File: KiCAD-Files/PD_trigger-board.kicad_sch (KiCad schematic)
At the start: 25 parts, among them J1 USB_C_Receptacle_USB2.0_14P, J10 15V, J11 18V, J2 Conn_01x03, J3 Conn_01x03, J4 VOUT, J5 5V, J6 5V, J7 5V, J8 9V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

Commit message: Routin fertig
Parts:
- removed Q1: AONR21307, Adafruit HUSB238 USB-C PD Breakout:POWERDI3333, symbol Adafruit HUSB238 USB-C PD Breakout-eagle-import:MOSFET-P-POWERDI3333
- added U2: SI4459ADY-T1-GE3, blinkyparts:SO_ADY-T1-GE3_VIS, symbol SI4459ADY:SI4459ADY-T1-GE3
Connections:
- net VBUS: now also U2.1 (S), U2.2 (S), U2.3 (S)
- net VOUT: now also U2.5 (D), U2.6 (D), U2.7 (D), U2.8 (D)
- net at R3.2, R4.1: now also U2.4 (G)
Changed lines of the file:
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@@
 	(paper "A4")
+	(junction
+		(at 236.22 105.41)
+		(diameter 0)
+		(color 0 0 0 0)
+	)
+	(junction
+		(at 236.22 35.56)
+		(diameter 0)
+		(color 0 0 0 0)
+	)
+	(junction
+		(at 274.32 87.63)
+		(diameter 0)
+		(color 0 0 0 0)
+	)
+	(junction
+		(at 254 35.56)
+		(diameter 0)
+		(color 0 0 0 0)
+	)
+	(junction
+		(at 274.32 96.52)
+		(diameter 0)
+		(color 0 0 0 0)
+	)
+	(junction
+		(at 236.22 87.63)
+		(diameter 0)
+		(color 0 0 0 0)
+	)
+	(junction
+		(at 175.26 138.43)
+		(diameter 0)
+		(color 0 0 0 0)
+	)
+	(junction
+		(at 274.32 105.41)
+		(diameter 0)
+		(color 0 0 0 0)
+	)
+	(junction
+		(at 55.88 88.9)
+		(diameter 0)
+		(color 0 0 0 0)
+	)
+	(junction
+		(at 148.59 127)
+		(diameter 0)
+		(color 0 0 0 0)
+	)
+	(junction
+		(at 226.06 45.72)
+		(diameter 0)
+		(color 0 0 0 0)
+	)
+	(junction
+		(at 243.84 35.56)
+		(diameter 0)
+		(color 0 0 0 0)
+	)
 	(junction
 		(at 214.63 35.56)
@@
 	)
 	(junction
-		(at 236.22 105.41)
-		(diameter 0)
-		(color 0 0 0 0)
-	)
-	(junction
-		(at 274.32 87.63)
-		(diameter 0)
-		(color 0 0 0 0)
-	)
-	(junction
-		(at 254 35.56)
-		(diameter 0)
-		(color 0 0 0 0)
-	)
-	(junction
-		(at 274.32 96.52)
-		(diameter 0)
-		(color 0 0 0 0)
-	)
-	(junction
-		(at 236.22 87.63)
-		(diameter 0)
-		(color 0 0 0 0)
-	)
-	(junction
-		(at 175.26 138.43)
-		(diameter 0)
-		(color 0 0 0 0)
-	)
-	(junction
-		(at 274.32 105.41)
-		(diameter 0)
-		(color 0 0 0 0)
-	)
-	(junction
-		(at 55.88 88.9)
-		(diameter 0)
-		(color 0 0 0 0)
-	)
-	(junction
-		(at 148.59 127)
+		(at 220.98 33.02)
 		(diameter 0)
 		(color 0 0 0 0)
@@
 	)
 	(junction
+		(at 236.22 30.48)
+		(diameter 0)
+		(color 0 0 0 0)
+	)
+	(junction
 		(at 264.16 35.56)
 		(diameter 0)
@@
 	)
 	(junction
-		(at 243.84 35.56)
+		(at 220.98 35.56)
 		(diameter 0)
 		(color 0 0 0 0)
@@
 	)
 	(junction
-		(at 226.06 45.72)
+		(at 236.22 33.02)
 		(diameter 0)
 		(color 0 0 0 0)
@@
 	(wire
 		(pts
+			(xy 220.98 33.02) (xy 220.98 35.56)
+		)
+		(stroke
+			(width 0)
+			(type default)
+		)
+	)
+	(wire
+		(pts
 			(xy 255.27 115.57) (xy 274.32 115.57)
 		)
@@
 	(wire
 		(pts
+			(xy 236.22 30.48) (xy 236.22 33.02)
+		)
+		(stroke
+			(width 0)
+			(type default)
+		)
+	)
+	(wire
+		(pts
 			(xy 148.59 120.65) (xy 148.59 127)
 		)
@@
 	(wire
 		(pts
+			(xy 236.22 33.02) (xy 236.22 35.56)
+		)
+		(stroke
+			(width 0)
+			(type default)
+		)
+	)
+	(wire
+		(pts
 			(xy 81.28 152.4) (xy 83.82 152.4)
 		)
@@
 	(wire
 		(pts
+			(xy 220.98 30.48) (xy 220.98 33.02)
+		)
+		(stroke
+			(width 0)
+			(type default)
+		)
+	)
+	(wire
+		(pts
 			(xy 236.22 87.63) (xy 236.22 96.52)
 		)
@@
 	(wire
 		(pts
+			(xy 236.22 27.94) (xy 236.22 30.48)
+		)
+		(stroke
+			(width 0)
+			(type default)
+		)
+	)
+	(wire
+		(pts
 			(xy 246.38 115.57) (xy 252.73 115.57)
 		)
@@
 	(wire
 		(pts
-			(xy 214.63 35.56) (xy 223.52 35.56)
+			(xy 226.06 40.64) (xy 226.06 45.72)
 		)
 		(stroke
@@
 	(wire
 		(pts
-			(xy 233.68 35.56) (xy 243.84 35.56)
-		)
-		(stroke
-			(width 0)
-			(type default)
-		)
-	)
-	(wire
-		(pts
 			(xy 236.22 105.41) (xy 236.22 115.57)
 		)
@@
 	(wire
 		(pts
+			(xy 236.22 35.56) (xy 243.84 35.56)
+		)
+		(stroke
+			(width 0)
+			(type default)
+		)
+	)
+	(wire
+		(pts
 			(xy 274.32 105.41) (xy 274.32 96.52)
 		)
@@
 	(wire
 		(pts
-			(xy 226.06 40.64) (xy 226.06 45.72)
-		)
-		(stroke
-			(width 0)
-			(type default)
-		)
-	)
-	(wire
-		(pts
 			(xy 264.16 35.56) (xy 273.05 35.56)
 		)
@@
 		(pts
 			(xy 130.81 80.01) (xy 130.81 82.55)
+		)
+		(stroke
+			(width 0)
+			(type default)
+		)
+	)
+	(wire
+		(pts
+			(xy 214.63 35.56) (xy 220.98 35.56)
 		)
 		(stroke
@@
 	)
 	(symbol
-		(lib_id "Adafruit HUSB238 USB-C PD Breakout-eagle-import:MOSFET-P-POWERDI3333")
-		(at 228.6 35.56 90)
-		(unit 1)
-		(exclude_from_sim no)
-		(in_bom yes)
-		(on_board yes)
-		(dnp no)
-		(property "Reference" "Q1"
-			(at 228.219 32.766 0)
-			(effects
-				(font
-					(size 1.27 1.0795)
-				)
-				(justify left bottom)
-			)
-		)
-		(property "Value" "AONR21307"
-			(at 230.505 32.766 0)
-			(effects
-				(font
-					(size 1.27 1.0795)
-				)
-				(justify left bottom)
-			)
-		)
-		(property "Footprint" "Adafruit HUSB238 USB-C PD Breakout:POWERDI3333"
-			(at 228.6 35.56 0)
-			(effects
-				(font
-					(size 1.27 1.27)
-				)
-				(hide yes)
-			)
-		)
-		(property "Datasheet" ""
-			(at 228.6 35.56 0)
-			(effects
-				(font
-					(size 1.27 1.27)
-				)
-				(hide yes)
-			)
-		)
-		(property "Description" ""
-			(at 228.6 35.56 0)
-			(effects
-				(font
-					(size 1.27 1.27)
-				)
-				(hide yes)
-			)
-		)
-		(pin "1"
-		)
-		(pin "2"
-		)
-		(pin "3"
-		)
-		(pin "4"
-		)
-		(pin "5678"
-		)
-		(instances
-			(project "PD_trigger-board"
-				(path "/e428d426-38f9-47e3-9715-a18ed772a1ec"
-					(reference "Q1")
-					(unit 1)
-				)
-			)
-		)
-	)
-	(symbol
 		(lib_id "power:GND")
 		(at 85.09 184.15 0)
@@
 					(unit 1)
 				)
+			)
+		)
+	)
+	(symbol
+		(lib_id "SI4459ADY:SI4459ADY-T1-GE3")
+		(at 226.06 40.64 90)
+		(unit 1)
+		(exclude_from_sim no)
+		(in_bom yes)
+		(on_board yes)
+		(dnp no)
+		(fields_autoplaced yes)
+		(property "Reference" "U2"
+			(at 228.6 22.86 90)
+			(effects
+				(font
+					(size 1.524 1.524)
+				)
+			)
+		)
+		(property "Value" "SI4459ADY-T1-GE3"
+			(at 228.6 25.4 90)
+			(effects
+				(font
+					(size 1.524 1.524)
+				)
+			)
+		)
+		(property "Footprint" "blinkyparts:SO_ADY-T1-GE3_VIS"
+			(at 226.06 40.64 0)
+			(effects
+				(font
+					(size 1.27 1.27)
+					(italic yes)
+				)
+				(hide yes)
+			)
+		)
+		(property "Datasheet" "SI4459ADY-T1-GE3"
+			(at 226.06 40.64 0)
+			(effects
+				(font
+					(size 1.27 1.27)
+					(italic yes)
+				)
+				(hide yes)
+			)
+		)
+		(property "Description" ""
+			(at 226.06 40.64 0)
+			(effects
+				(font
+					(size 1.27 1.27)
+				)
+				(hide yes)
+			)
+		)
+		(pin "2"
+		)
+		(pin "4"
+		)
+		(pin "1"
+		)
+		(pin "7"
+		)
+		(pin "6"
+		)
+		(pin "5"
+		)
+		(pin "3"
+		)
+		(pin "8"
+		)
+		(instances
+			(project ""
+				(path "/e428d426-38f9-47e3-9715-a18ed772a1ec"
+					(reference "U2")
+					(unit 1)
+				)

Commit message: Partlist fertig
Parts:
- C1: FCSC (none) -> C15849
- C2, C3, C4: value C -> 4.7uF 35V; FCSC (none) -> C307467
- J1: value USB_C_Receptacle_USB2.0_14P -> USB_C_Receptacle_USB3.0_12P
- R1: FCSC (none) -> C25139
- R2, R7: FCSC (none) -> C54831
- R3: FCSC (none) -> C100457
- R4: FCSC (none) -> C25941
- R5: value 6k -> 6.04k; FCSC (none) -> C25913
- R6: FCSC (none) -> C25531
- R8: FCSC (none) -> C25542
- U1: FCSC (none) -> C7471904
- U2: FCSC (none) -> C143743
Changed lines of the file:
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@@
+			)
+		)
+		(property "FCSC" "C25531"
+			(at 242.57 96.52 90)
+			(effects
+				(font
+					(size 1.27 1.27)
+				)
+				(hide yes)
 			)
 		)
@@
 			)
 		)
-		(property "Value" "C"
+		(property "Value" "4.7uF 35V"
 			(at 257.81 40.6399 0)
 			(effects
@@
 			)
 		)
+		(property "FCSC" "C307467"
+			(at 254 39.37 0)
+			(effects
+				(font
+					(size 1.27 1.27)
+				)
+				(hide yes)
+			)
+		)
 		(pin "1"
 		)
@@
 			)
 		)
+		(property "FCSC" "C25941"
+			(at 226.06 52.07 0)
+			(effects
+				(font
+					(size 1.27 1.27)
+				)
+				(hide yes)
+			)
+		)
 		(pin "2"
 		)
@@
 			)
 		)
+		(property "FCSC" "C100457"
+			(at 214.63 41.91 0)
+			(effects
+				(font
+					(size 1.27 1.27)
+				)
+				(hide yes)
+			)
+		)
 		(pin "2"
 		)
@@
 			)
 		)
-		(property "Value" "C"
+		(property "Value" "4.7uF 35V"
 			(at 247.65 40.6399 0)
 			(effects
@@
 			)
 		)
+		(property "FCSC" "C307467"
+			(at 243.84 39.37 0)
+			(effects
+				(font
+					(size 1.27 1.27)
+				)
+				(hide yes)
+			)
+		)
 		(pin "1"
 		)
@@
 			)
 		)
-		(property "Value" "USB_C_Receptacle_USB2.0_14P"
+		(property "Value" "USB_C_Receptacle_USB3.0_12P"
 			(at 40.64 64.77 0)
 			(effects
@@
 			)
 		)
-		(property "Description" "USB 2.0-only 14P Type-C Receptacle connector"
-			(at 40.64 85.09 0)
-			(effects
-				(font
-					(size 1.27 1.27)
-				)
-				(hide yes)
-			)
-		)
-		(property "LCSC" ""
+		(property "Description" "USB 3.0-only 12P Type-C Receptacle connector"
 			(at 40.64 85.09 0)
 			(effects
@@
 			)
 		)
-		(property "Description" ""
+		(property "Description" "P-Channel MOSFET"
 			(at 226.06 40.64 0)
+			(effects
+				(font
+					(size 1.27 1.27)
+				)
+				(hide yes)
+			)
+		)
+		(property "FCSC" "C143743"
+			(at 226.06 40.64 90)
 			(effects
 				(font
@@
 			)
 		)
+		(property "FCSC" "C7471904"
+			(at 170.18 88.9 0)
+			(effects
+				(font
+					(size 1.27 1.27)
+				)
+				(hide yes)
+			)
+		)
 		(pin "8"
 		)
@@
 			)
 		)
-		(property "Value" "C"
+		(property "Value" "4.7uF 35V"
 			(at 267.97 40.6399 0)
 			(effects
@@
 			)
 		)
+		(property "FCSC" "C307467"
+			(at 264.16 39.37 0)
+			(effects
+				(font
+					(size 1.27 1.27)
+				)
+				(hide yes)
+			)
+		)
 		(pin "1"
 		)
@@
 			)
 		)
+		(property "FCSC" "C25542"
+			(at 242.57 115.57 90)
+			(effects
+				(font
+					(size 1.27 1.27)
+				)
+				(hide yes)
+			)
+		)
 		(pin "2"
 		)
@@
 			)
 		)
+		(property "FCSC" "C15849"
+			(at 130.81 76.2 0)
+			(effects
+				(font
+					(size 1.27 1.27)
+				)
+				(hide yes)
+			)
+		)
 		(pin "1"
 		)
@@
 			)
 		)
+		(property "FCSC" "C54831"
+			(at 242.57 105.41 90)
+			(effects
+				(font
+					(size 1.27 1.27)
+				)
+				(hide yes)
+			)
+		)
 		(pin "2"
 		)
@@
 			)
 		)
+		(property "FCSC" "C25139"
+			(at 130.81 64.77 0)
+			(effects
+				(font
+					(size 1.27 1.27)
+				)
+				(hide yes)
+			)
+		)
 		(pin "2"
 		)
@@
 			)
 		)
-		(property "Value" "6k"
+		(property "Value" "6.04k"
 			(at 242.57 83.82 90)
 			(effects
@@
 			)
 		)
+		(property "FCSC" "C25913"
+			(at 242.57 87.63 90)
+			(effects
+				(font
+					(size 1.27 1.27)
+				)
+				(hide yes)
+			)
+		)
 		(pin "2"
 		)
@@
 			(effects
 				(font
+					(size 1.27 1.27)
+				)
+				(hide yes)
+			)
+		)
+		(property "FCSC" "C54831"
+			(at 156.21 138.43 90)
+			(effects
+				(font

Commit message: minor changes for v0.1
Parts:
- J1: FCSC (none) -> C136423
- J10, J11, J2, J3, J4, J5, J6, J7, J8, J9: now not fitted
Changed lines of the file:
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@@
 		(in_bom yes)
 		(on_board yes)
-		(dnp no)
+		(dnp yes)
 		(fields_autoplaced yes)
 		(property "Reference" "J7"
@@
 			)
 		)
+		(property "FCSC" "C136423"
+			(at 40.64 85.09 0)
+			(effects
+				(font
+					(size 1.27 1.27)
+				)
+				(hide yes)
+			)
+		)
 		(pin "A6"
 		)
@@
 		(in_bom yes)
 		(on_board yes)
-		(dnp no)
+		(dnp yes)
 		(fields_autoplaced yes)
 		(property "Reference" "J3"
@@
 		(in_bom yes)
 		(on_board yes)
-		(dnp no)
+		(dnp yes)
 		(fields_autoplaced yes)
 		(property "Reference" "J2"
@@
 		(in_bom yes)
 		(on_board yes)
-		(dnp no)
+		(dnp yes)
 		(fields_autoplaced yes)
 		(property "Reference" "J8"
@@
 		(in_bom yes)
 		(on_board yes)
-		(dnp no)
+		(dnp yes)
 		(fields_autoplaced yes)
 		(property "Reference" "J11"
@@
 		(in_bom yes)
 		(on_board yes)
-		(dnp no)
+		(dnp yes)
 		(fields_autoplaced yes)
 		(property "Reference" "J5"
@@
 		(in_bom yes)
 		(on_board yes)
-		(dnp no)
+		(dnp yes)
 		(fields_autoplaced yes)
 		(property "Reference" "J9"
@@
 		(in_bom yes)
 		(on_board yes)
-		(dnp no)
+		(dnp yes)
 		(fields_autoplaced yes)
 		(property "Reference" "J6"
@@
 		(in_bom yes)
 		(on_board yes)
-		(dnp no)
+		(dnp yes)
 		(fields_autoplaced yes)
 		(property "Reference" "J10"
@@
 		(in_bom yes)
 		(on_board yes)
-		(dnp no)
+		(dnp yes)
 		(fields_autoplaced yes)
 		(property "Reference" "J4"

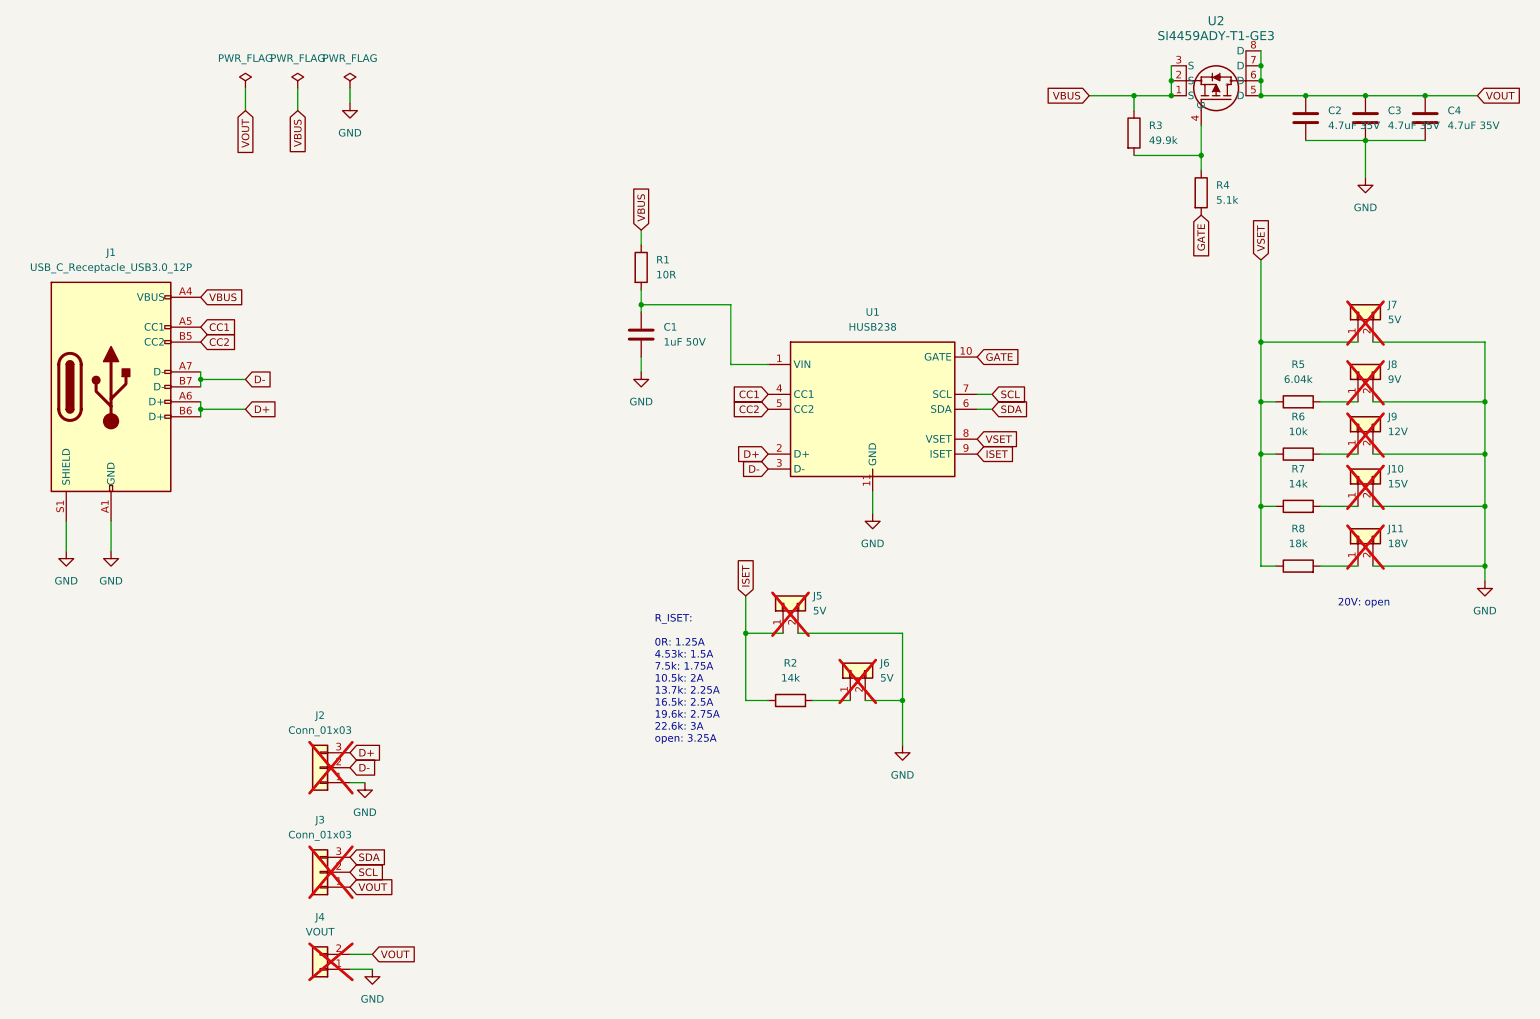
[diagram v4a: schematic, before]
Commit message: first draft of new layout
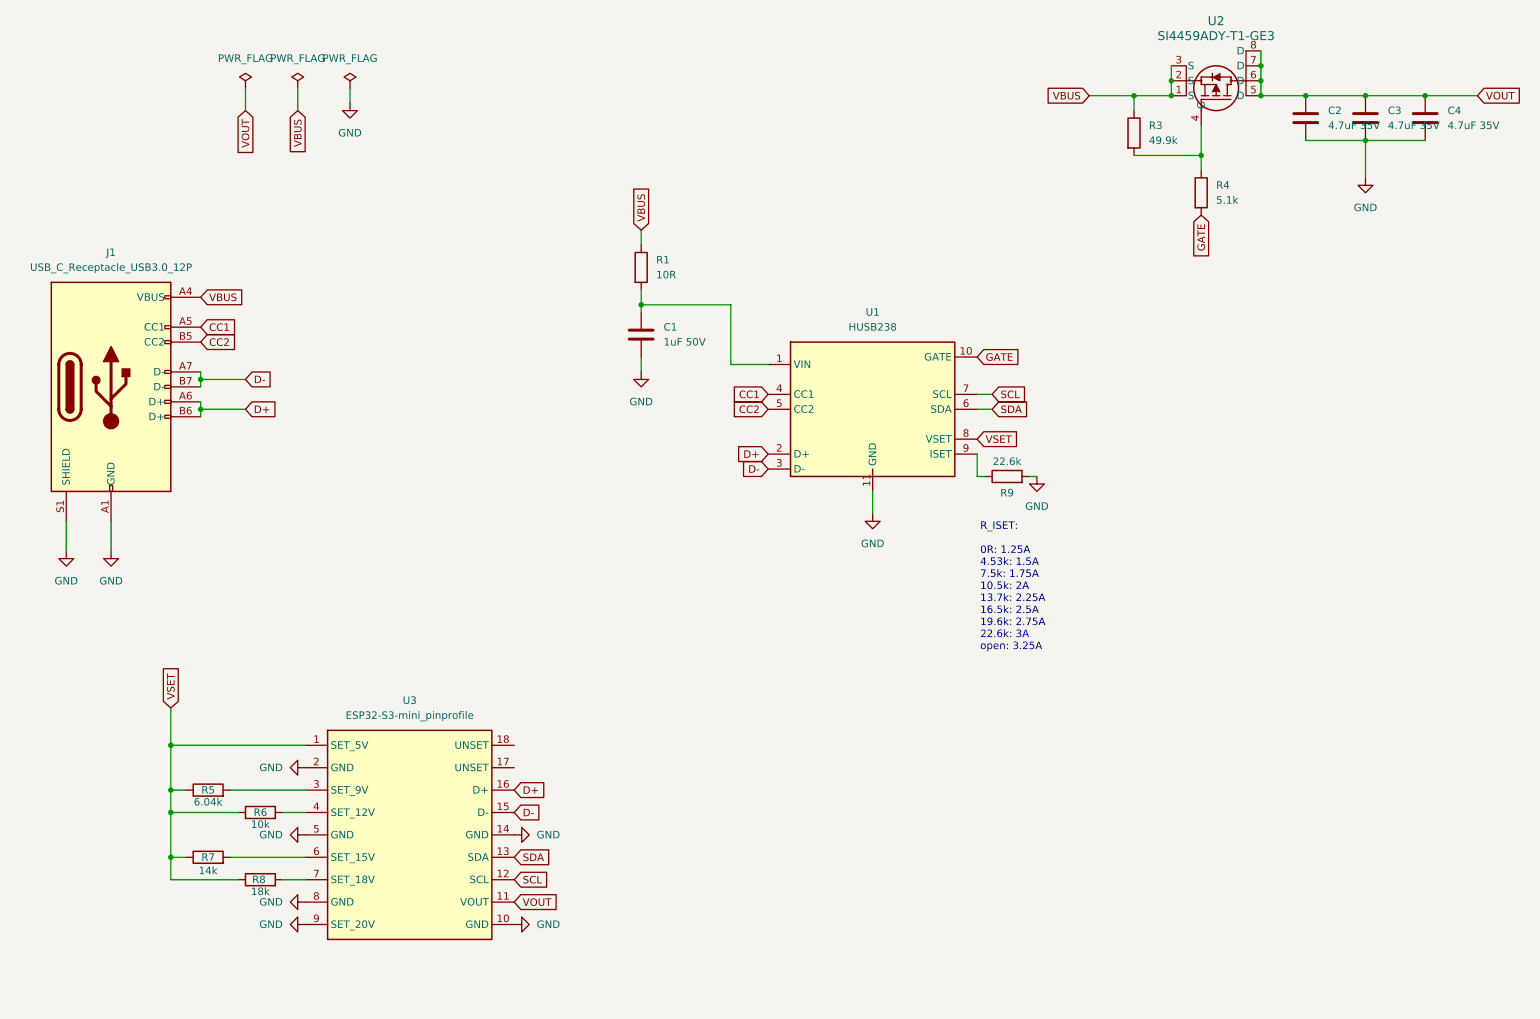
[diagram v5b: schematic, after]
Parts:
- removed J10: 15V, Connector_PinHeader_2.54mm:PinHeader_1x02_P2.54mm_Vertical, symbol Connector_Generic:Conn_01x02
- removed J11: 18V, Connector_PinHeader_2.54mm:PinHeader_1x02_P2.54mm_Vertical, symbol Connector_Generic:Conn_01x02
- removed J2, J3: Conn_01x03, Connector_PinHeader_2.54mm:PinHeader_1x03_P2.54mm_Vertical, symbol Connector_Generic:Conn_01x03
- removed J4: VOUT, TerminalBlock:TerminalBlock_bornier-2_P5.08mm, symbol Connector_Generic:Conn_01x02
- removed J5, J6, J7: 5V, Connector_PinHeader_2.54mm:PinHeader_1x02_P2.54mm_Vertical, symbol Connector_Generic:Conn_01x02
- removed J8: 9V, Connector_PinHeader_2.54mm:PinHeader_1x02_P2.54mm_Vertical, symbol Connector_Generic:Conn_01x02
- removed J9: 12V, Connector_PinHeader_2.54mm:PinHeader_1x02_P2.54mm_Vertical, symbol Connector_Generic:Conn_01x02
- removed R2: 14k, Resistor_SMD:R_0402_1005Metric, symbol Device:R
- added R9: 22.6k, Resistor_SMD:R_0402_1005Metric, symbol Device:R
- added U3: ESP32-S3-mini_pinprofile, blinkyparts:ESP32-S3-Zero, symbol blinkyparts:ESP32-S3-mini_pinprofile
- J1: footprint Connector_USB:USB_C_Receptacle_HRO_TYPE-C-31-M-12 -> Connector_USB:USB_C_Receptacle_GCT_USB4110
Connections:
- net D+: now also U3.16 (D+)
- net D-: now also U3.15 (D-)
- net GND: now also R9.2, U3.10 (GND), U3.14 (GND), U3.2 (GND), U3.5 (GND), U3.8 (GND), U3.9 (SET_20V)
- net SCL: now also U3.12 (SCL)
- net SDA: now also U3.13 (SDA)
- net VOUT: now also U3.11 (VOUT)
- net VSET: now also U3.1 (SET_5V)
- net at R6.2: now also U3.4 (SET_12V)
- net at R5.2: now also U3.3 (SET_9V)
- net at R8.2: now also U3.7 (SET_18V)
- net at R7.2: now also U3.6 (SET_15V)
- net ISET: no longer names the net of U1.9 (ISET)
- net ISET: now also R9.1
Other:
- note removed: "20V: open"
